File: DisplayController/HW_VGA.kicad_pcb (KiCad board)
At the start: 2 copper layers, 150 x 90 mm, 77 parts, among them J1 Conn_02x40_Odd_Even, J301 Conn_01x02, J401 Conn_01x06, U102 GAL22V10, U103 74ALS163, U104 74ALS163, U105 74ALS163, U202 GAL22V10, U203 74ALS163, U204 74ALS163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

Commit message: fixed one isolated ground
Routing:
- net GND: track 56.9 -> 60.8 mm, vias 45 -> 49
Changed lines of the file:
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@@
+	)
+	(via
+		(at 69 122.9)
+		(size 0.6)
+		(drill 0.3)
+		(layers "F.Cu" "B.Cu")
+		(free yes)
+		(net 2)
 	)
 	(via
@@
 	)
 	(via
+		(at 71.821 119.275)
+		(size 0.6)
+		(drill 0.3)
+		(layers "F.Cu" "B.Cu")
+		(net 2)
+	)
+	(via
+		(at 111.5 119.2)
+		(size 0.6)
+		(drill 0.3)
+		(layers "F.Cu" "B.Cu")
+		(net 2)
+	)
+	(via
 		(at 111.6 116.625)
 		(size 0.6)
@@
 	(via
 		(at 135.075 100.7)
+		(size 0.6)
+		(drill 0.3)
+		(layers "F.Cu" "B.Cu")
+		(free yes)
+		(net 2)
+	)
+	(via
+		(at 76.025 122.85)
 		(size 0.6)
 		(drill 0.3)
@@
 	)
 	(segment
+		(start 71.375 115.5725)
+		(end 71.375 118.829)
+		(width 0.6)
+		(layer "B.Cu")
+		(net 2)
+	)
+	(segment
 		(start 93.7575 121.4675)
 		(end 93.725 121.5)
 		(width 0.6)
 		(layer "B.Cu")
+		(net 2)
+	)
+	(segment
+		(start 71.375 118.829)
+		(end 71.821 119.275)
+		(width 0.6)
+		(layer "B.Cu")

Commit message: fix more unconnected grounds
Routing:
- net GND: track 60.8 -> 62.9 mm, vias 49 -> 60
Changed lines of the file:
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@@
+	)
+	(segment
+		(start 191.625 118.078001)
+		(end 191.6 118.103001)
+		(width 0.6)
+		(layer "F.Cu")
+		(net 2)
 	)
 	(segment
@@
 	)
 	(segment
+		(start 191.625 117.56)
+		(end 191.625 118.078001)
+		(width 0.6)
+		(layer "F.Cu")
+		(net 2)
+	)
+	(segment
 		(start 176.925 111.25)
 		(end 176.925 110.577)
@@
 	)
 	(segment
+		(start 191.625 120.1)
+		(end 193.2 120.1)
+		(width 0.6)
+		(layer "F.Cu")
+		(net 2)
+	)
+	(segment
 		(start 117.5 116.625)
 		(end 111.6 116.625)
@@
 	)
 	(via
+		(at 161.85 135.125)
+		(size 0.6)
+		(drill 0.3)
+		(layers "F.Cu" "B.Cu")
+		(free yes)
+		(net 2)
+	)
+	(via
 		(at 175.1 88.75)
 		(size 0.6)
@@
 	)
 	(via
+		(at 193.2 120.1)
+		(size 0.6)
+		(drill 0.3)
+		(layers "F.Cu" "B.Cu")
+		(net 2)
+	)
+	(via
 		(at 204.7 113.625)
 		(size 0.6)
@@
 	)
 	(via
+		(at 192.525 115.025)
+		(size 0.6)
+		(drill 0.3)
+		(layers "F.Cu" "B.Cu")
+		(net 2)
+	)
+	(via
 		(at 93.725 121.5)
 		(size 0.6)
@@
 	)
 	(via
+		(at 162.05 128.95)
+		(size 0.6)
+		(drill 0.3)
+		(layers "F.Cu" "B.Cu")
+		(free yes)
+		(net 2)
+	)
+	(via
 		(at 131.425 102.05)
 		(size 0.6)
@@
 	)
 	(via
+		(at 162.55 108.775)
+		(size 0.6)
+		(drill 0.3)
+		(layers "F.Cu" "B.Cu")
+		(free yes)
+		(net 2)
+	)
+	(via
 		(at 202.35 118.103001)
 		(size 0.6)
@@
 	)
 	(via
+		(at 191.6 118.103001)
+		(size 0.6)
+		(drill 0.3)
+		(layers "F.Cu" "B.Cu")
+		(net 2)
+	)
+	(via
 		(at 76.025 122.85)
 		(size 0.6)
@@
 	)
 	(via
+		(at 162.525 113.075)
+		(size 0.6)
+		(drill 0.3)
+		(layers "F.Cu" "B.Cu")
+		(free yes)
+		(net 2)
+	)
+	(via
 		(at 117.5 116.625)
 		(size 0.6)
@@
 	)
 	(via
+		(at 165.45 135.125)
+		(size 0.6)
+		(drill 0.3)
+		(layers "F.Cu" "B.Cu")
+		(free yes)
+		(net 2)
+	)
+	(via
 		(at 185.275 128.725)
 		(size 0.6)
@@
 	)
 	(via
+		(at 162.425 117.625)
+		(size 0.6)
+		(drill 0.3)
+		(layers "F.Cu" "B.Cu")
+		(free yes)
+		(net 2)
+	)
+	(via
 		(at 179.45 128.725)
 		(size 0.6)
@@
 	)
 	(via
+		(at 165.45 128.925)
+		(size 0.6)
+		(drill 0.3)
+		(layers "F.Cu" "B.Cu")
+		(free yes)
+		(net 2)
+	)
+	(via
 		(at 138.175 100.75)
 		(size 0.6)
@@
 		(net 2)
 	)
+	(via
+		(at 192.45 113.75)
+		(size 0.6)
+		(drill 0.3)
+		(layers "F.Cu" "B.Cu")
+		(net 2)
+	)

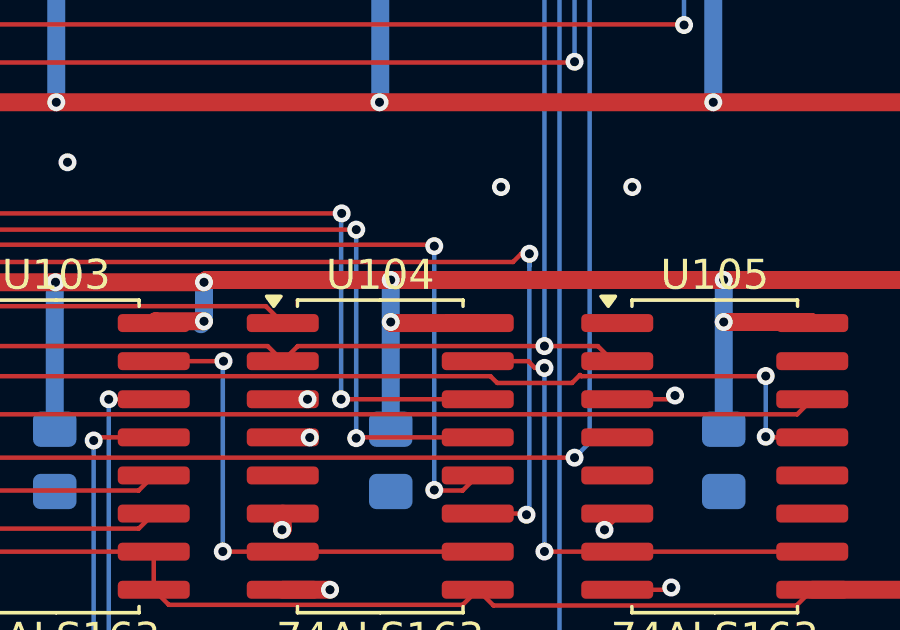
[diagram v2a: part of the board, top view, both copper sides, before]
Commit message: fixed a missing signal
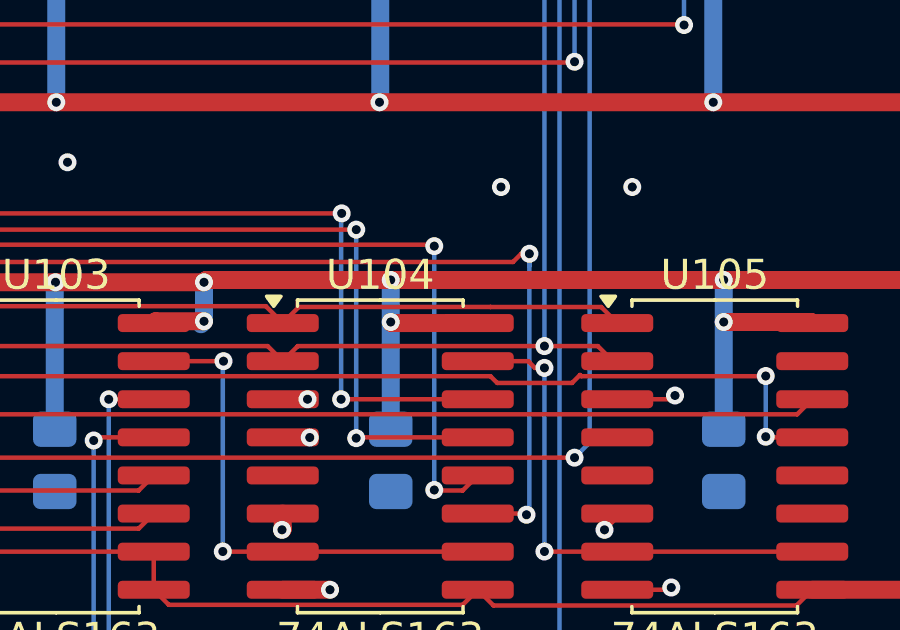
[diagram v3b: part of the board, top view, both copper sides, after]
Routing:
- net /HCount/-HCOUNT_CLR: track 26.7 -> 38.3 mm
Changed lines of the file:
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@@
+	)
+	(segment
+		(start 202.24 110.675)
+		(end 202.775 111.21)
+		(width 0.15)
+		(layer "F.Cu")
+		(net 108)
 	)
 	(segment
@@
 		(start 169.956 111.752)
 		(end 169.954 111.75)
+		(width 0.15)
+		(layer "F.Cu")
+		(net 108)
+	)
+	(segment
+		(start 198.548 110.673)
+		(end 198.55 110.675)
 		(width 0.15)
 		(layer "F.Cu")
@@
 	)
 	(segment
+		(start 198.55 110.675)
+		(end 202.24 110.675)
+		(width 0.15)
+		(layer "F.Cu")
+		(net 108)
+	)
+	(segment
+		(start 192.162 110.673)
+		(end 198.548 110.673)
+		(width 0.15)
+		(layer "F.Cu")
+		(net 108)
+	)
+	(segment
 		(start 191.063 110.648)
 		(end 181.387 110.648)
@@
 		(width 0.15)
 		(layer "F.Cu")
+		(net 108)
+	)
+	(segment
+		(start 191.625 111.21)
+		(end 192.162 110.673)
+		(width 0.15)
+		(layer "F.Cu")

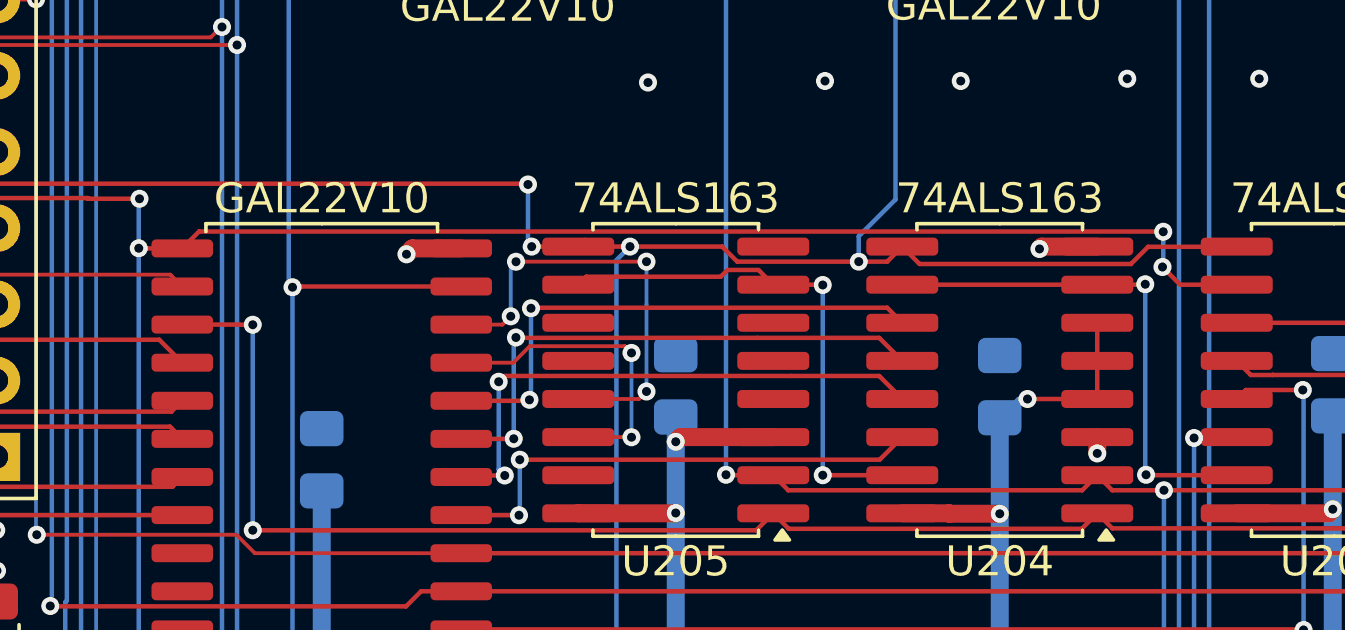
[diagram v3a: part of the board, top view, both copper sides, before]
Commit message: fix more unconnected grounds
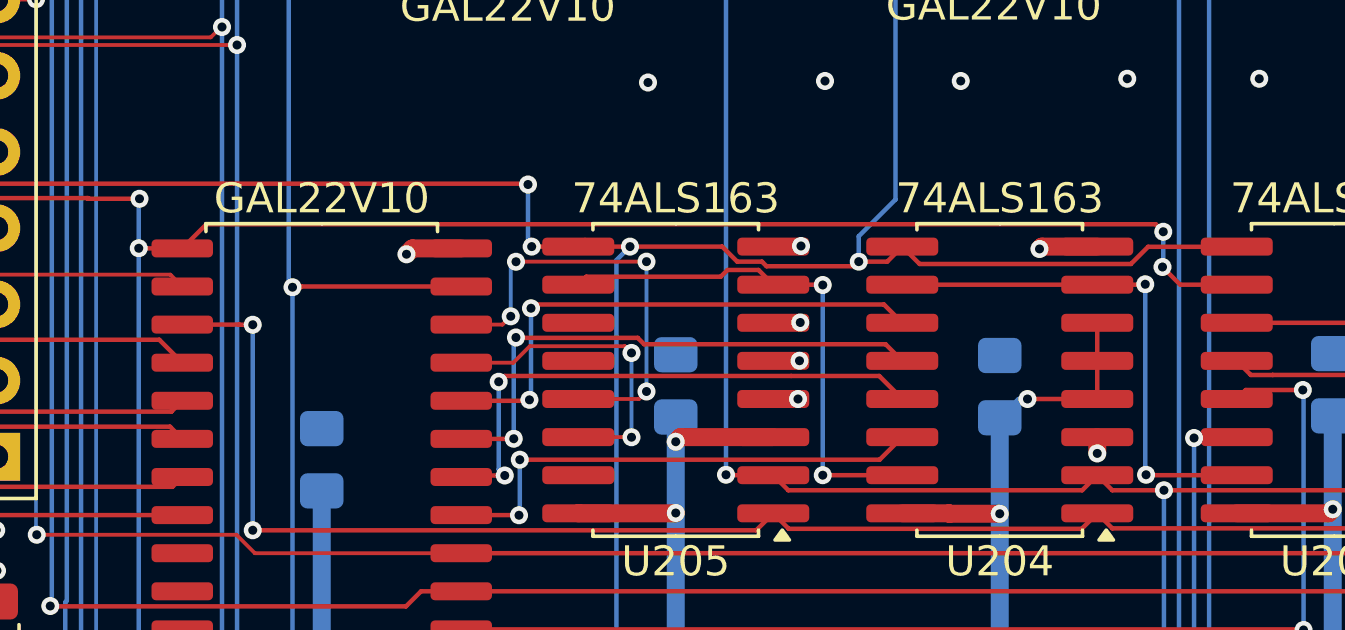
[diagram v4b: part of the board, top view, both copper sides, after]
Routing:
- net GND: vias 60 -> 64
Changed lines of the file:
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@@
 	)
 	(via
+		(at 188.25 88.475)
+		(size 0.6)
+		(drill 0.3)
+		(layers "F.Cu" "B.Cu")
+		(net 2)
+	)
+	(via
+		(at 188.225 91.025)
+		(size 0.6)
+		(drill 0.3)
+		(layers "F.Cu" "B.Cu")
+		(net 2)
+	)
+	(via
 		(at 130.3 96.45)
 		(size 0.6)
@@
 	)
 	(via
+		(at 188.15 93.575)
+		(size 0.6)
+		(drill 0.3)
+		(layers "F.Cu" "B.Cu")
+		(net 2)
+	)
+	(via
 		(at 189.05 82.975)
 		(size 0.6)
@@
 	)
 	(via
+		(at 188.2 92.3)
+		(size 0.6)
+		(drill 0.3)
+		(layers "F.Cu" "B.Cu")
+		(net 2)
+	)
+	(via
 		(at 199.2 124.125)
 		(size 0.6)
@@
 	)
 	(segment
-		(start 185.63902 88.51098)
-		(end 185.62304 88.495)
+		(start 127.69806 86.373)
+		(end 127.684962 86.359902)
 		(width 0.15)
 		(layer "F.Cu")
@@
 	)
 	(segment
-		(start 127.69806 86.373)
-		(end 127.684962 86.359902)
+		(start 112.7 67.85)
+		(end 127.675 67.85)
 		(width 0.15)
 		(layer "F.Cu")
@@
 	)
 	(segment
-		(start 112.7 67.85)
-		(end 127.675 67.85)
+		(start 190.175 88.997)
+		(end 190.022 89.15)
 		(width 0.15)
 		(layer "F.Cu")
@@
 	)
 	(segment
+		(start 190.022 89.15)
+		(end 187.101738 89.15)
+		(width 0.15)
+		(layer "F.Cu")
+		(net 65)
+	)
+	(segment
 		(start 182.55 88.495)
 		(end 182.555 88.5)
@@
 	)
 	(segment
-		(start 127.675 67.85)
-		(end 127.7 67.875)
+		(start 187.101738 89.15)
+		(end 186.948738 88.997)
 		(width 0.15)
 		(layer "F.Cu")
@@
 	)
 	(segment
-		(start 190.175 88.997)
-		(end 186.12504 88.997)
+		(start 186.12504 88.997)
+		(end 185.62304 88.495)
+		(width 0.15)
+		(layer "F.Cu")
+		(net 65)
+	)
+	(segment
+		(start 127.675 67.85)
+		(end 127.7 67.875)
 		(width 0.15)
 		(layer "F.Cu")
@@
 	)
 	(segment
+		(start 186.948738 88.997)
+		(end 186.12504 88.997)
+		(width 0.15)
+		(layer "F.Cu")
+		(net 65)
+	)
+	(segment
 		(start 191.123 88.997)
 		(end 190.175 88.997)
@@
 	)
 	(segment
-		(start 186.12504 88.997)
-		(end 185.63902 88.51098)
-		(width 0.15)
-		(layer "F.Cu")
-		(net 65)
-	)
-	(segment
 		(start 190.025 64.83)
 		(end 189.543 64.348)
@@
 	)
 	(segment
-		(start 185.62304 88.495)
-		(end 182.55 88.495)
-		(width 0.15)
-		(layer "F.Cu")
-		(net 65)
-	)
-	(segment
 		(start 158.125 86.375)
 		(end 158.123 86.373)
@@
 		(net 65)
 	)
+	(segment
+		(start 185.62304 88.495)
+		(end 182.55 88.495)
+		(width 0.15)
+		(layer "F.Cu")
+		(net 65)
+	)
 	(via
 		(at 112.723 76.275)
@@
 	)
 	(segment
-		(start 164.45 86.878)
-		(end 128.201 86.878)
-		(width 0.15)
-		(layer "F.Cu")
-		(net 105)
-	)
-	(segment
-		(start 168.187 87.993)
-		(end 200.318 87.993)
+		(start 168.43 87.75)
+		(end 200.075 87.75)
 		(width 0.15)
 		(layer "F.Cu")
@@
 	)
 	(segment
-		(start 200.318 87.993)
-		(end 200.325 88)
+		(start 164.45 86.878)
+		(end 128.201 86.878)
 		(width 0.15)
 		(layer "F.Cu")
@@
 	)
 	(segment
+		(start 200.075 87.75)
+		(end 200.325 88)
+		(width 0.15)
+		(layer "F.Cu")
+		(net 105)
+	)
+	(segment
 		(start 166.2 86.9)
 		(end 164.472 86.9)
@@
 	)
 	(segment
-		(start 200.3 89.175)
-		(end 200.89 89.765)
+		(start 167.625 88.555)
+		(end 168.43 87.75)
 		(width 0.15)
 		(layer "F.Cu")
@@
 	)
 	(segment
-		(start 167.625 88.555)
-		(end 168.187 87.993)
+		(start 200.3 89.175)
+		(end 200.89 89.765)
 		(width 0.15)
 		(layer "F.Cu")
@@
 	(segment
 		(start 191.625 91.035)
-		(end 191.123 90.533)
+		(end 191.015 90.425)
 		(width 0.15)
 		(layer "F.Cu")
@@
 	)
 	(segment
-		(start 191.123 90.533)
-		(end 179.267 90.533)
+		(start 179.165902 93.635)
+		(end 176.925 93.635)
 		(width 0.15)
 		(layer "F.Cu")
@@
 	)
 	(segment
-		(start 179.165902 93.635)
-		(end 176.925 93.635)
+		(start 179.198001 93.602901)
+		(end 179.165902 93.635)
 		(width 0.15)
 		(layer "F.Cu")
@@
 	)
 	(segment
-		(start 179.267 90.533)
-		(end 179.25 90.55)
+		(start 191.015 90.425)
+		(end 179.375 90.425)
 		(width 0.15)
 		(layer "F.Cu")
@@
 	)
 	(segment
-		(start 179.198001 93.602901)
-		(end 179.165902 93.635)
+		(start 179.375 90.425)
+		(end 179.25 90.55)
 		(width 0.15)
 		(layer "F.Cu")
@@
 	)
 	(segment
-		(start 178.76 91.537)
-		(end 178.748 91.525)
+		(start 182.807936 91.537)
+		(end 178.76 91.537)
 		(width 0.15)
 		(layer "F.Cu")
@@
 	)
 	(segment
-		(start 186.8 91.537)
-		(end 178.76 91.537)
+		(start 191.625 92.305)
+		(end 191.07 91.75)
 		(width 0.15)
 		(layer "F.Cu")
@@
 	)
 	(segment
-		(start 190.857 91.537)
-		(end 186.8 91.537)
+		(start 183.020936 91.75)
+		(end 182.807936 91.537)
 		(width 0.15)
 		(layer "F.Cu")
@@
 	)
 	(segment
-		(start 191.625 92.305)
-		(end 190.857 91.537)
+		(start 191.07 91.75)
+		(end 183.020936 91.75)
+		(width 0.15)
+		(layer "F.Cu")
+		(net 126)
+	)
+	(segment
+		(start 178.76 91.537)
+		(end 178.748 91.525)
 		(width 0.15)
 		(layer "F.Cu")

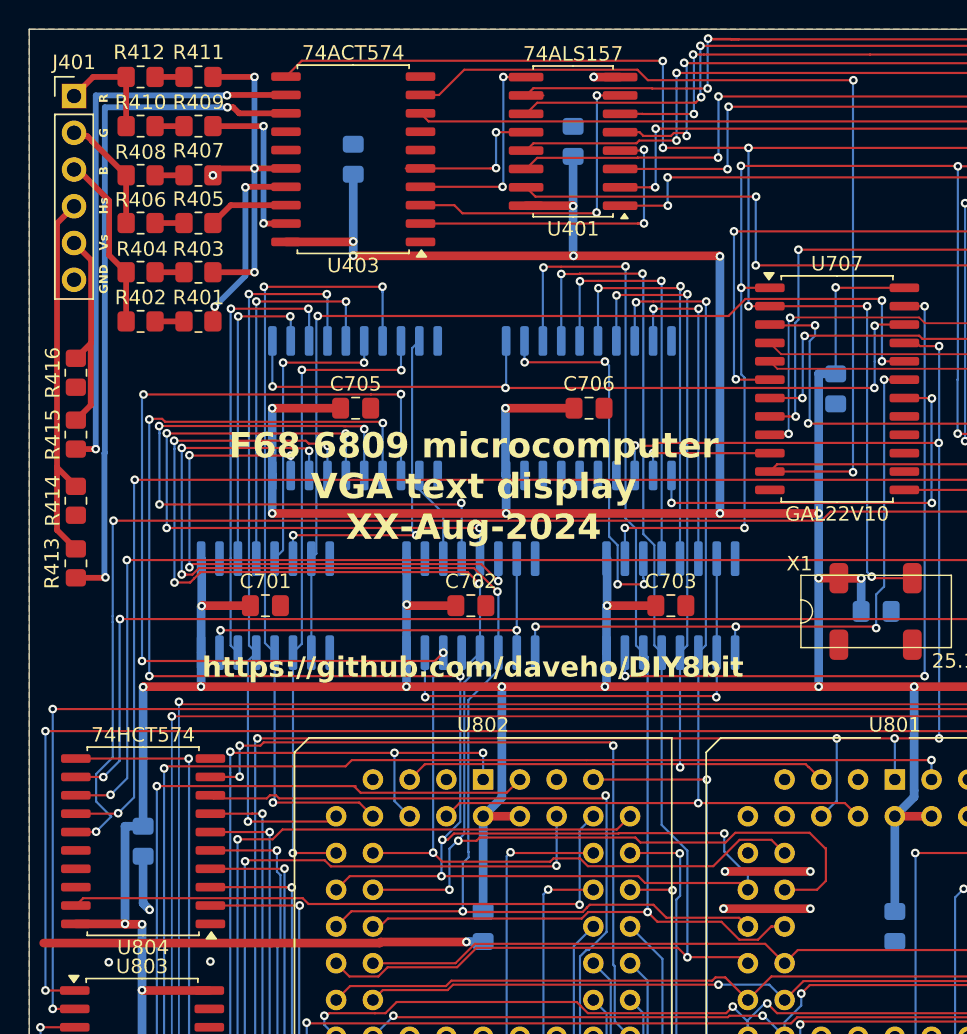
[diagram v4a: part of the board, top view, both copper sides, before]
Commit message: fixing more unrouted ground connections
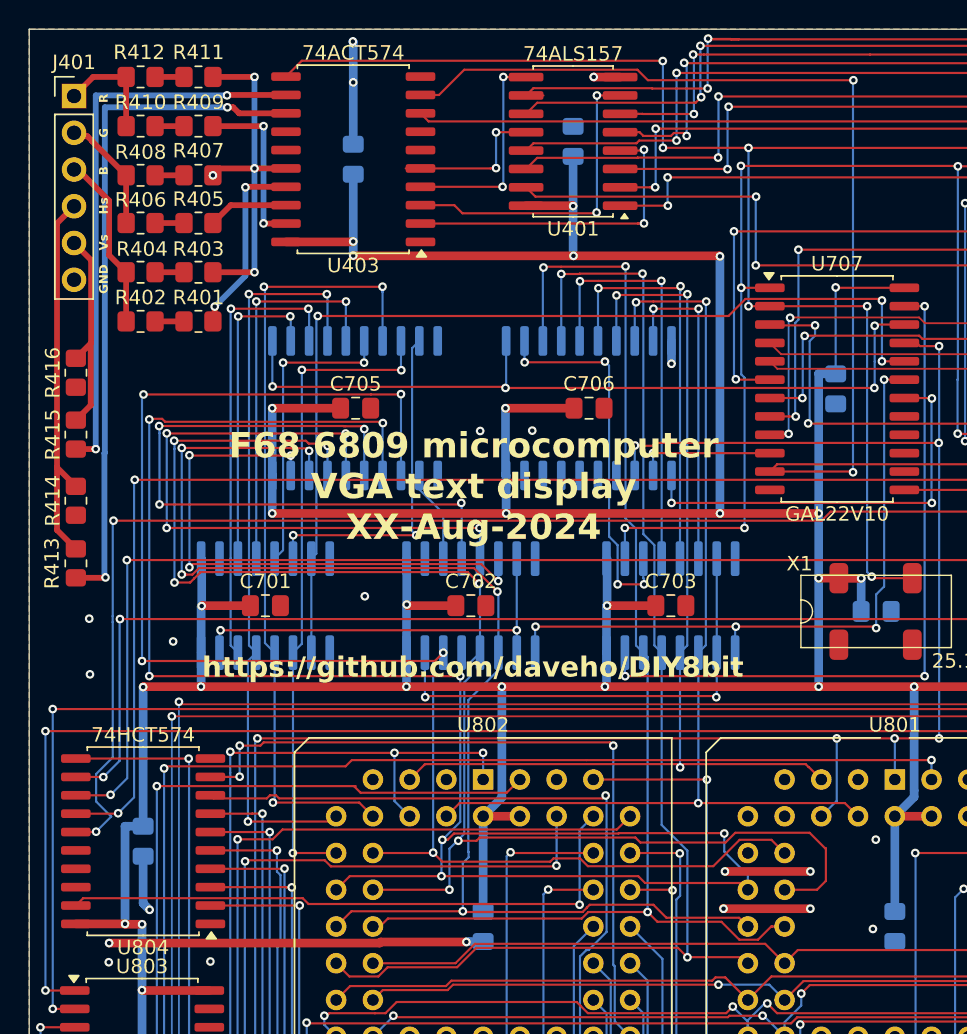
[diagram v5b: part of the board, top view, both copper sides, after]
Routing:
- net GND: track 62.9 -> 67.1 mm, vias 64 -> 76
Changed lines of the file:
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@@
-	)
-	(segment
-		(start 93.725 121.5)
-		(end 87.799658 121.5)
-		(width 0.6)
-		(layer "F.Cu")
-		(net 2)
 	)
 	(segment
@@
 	)
 	(segment
+		(start 87.799658 121.5)
+		(end 87.724658 121.575)
+		(width 0.6)
+		(layer "F.Cu")
+		(net 2)
+	)
+	(segment
 		(start 198.125 94.845)
 		(end 198.125 95.388001)
-		(width 0.6)
-		(layer "F.Cu")
-		(net 2)
-	)
-	(segment
-		(start 87.799658 121.5)
-		(end 87.724658 121.575)
 		(width 0.6)
 		(layer "F.Cu")
@@
 	)
 	(segment
+		(start 93.725 121.5)
+		(end 87.799658 121.5)
+		(width 0.6)
+		(layer "F.Cu")
+		(net 2)
+	)
+	(segment
 		(start 202.775 117.678001)
 		(end 202.35 118.103001)
@@
 	)
 	(segment
-		(start 80.25 121.575)
-		(end 64.5 121.575)
-		(width 0.6)
-		(layer "F.Cu")
-		(net 2)
-	)
-	(segment
-		(start 87.724658 121.575)
-		(end 80.25 121.575)
-		(width 0.6)
-		(layer "F.Cu")
-		(net 2)
-	)
-	(segment
 		(start 117.5 119.2)
 		(end 111.5 119.2)
@@
 		(net 2)
 	)
+	(segment
+		(start 69.025 121.575)
+		(end 87.724658 121.575)
+		(width 0.6)
+		(layer "F.Cu")
+		(net 2)
+	)
 	(via
 		(at 185.275 134.9)
@@
 	)
 	(via
+		(at 121.825 120.6)
+		(size 0.6)
+		(drill 0.3)
+		(layers "F.Cu" "B.Cu")
+		(free yes)
+		(net 2)
+	)
+	(via
 		(at 188.225 91.025)
 		(size 0.6)
@@
 	)
 	(via
+		(at 98.275 86.15)
+		(size 0.6)
+		(drill 0.3)
+		(layers "F.Cu" "B.Cu")
+		(free yes)
+		(net 2)
+	)
+	(via
+		(at 67.65 99.15)
+		(size 0.6)
+		(drill 0.3)
+		(layers "F.Cu" "B.Cu")
+		(free yes)
+		(net 2)
+	)
+	(via
+		(at 94.675 86.175)
+		(size 0.6)
+		(drill 0.3)
+		(layers "F.Cu" "B.Cu")
+		(free yes)
+		(net 2)
+	)
+	(via
 		(at 130.3 96.45)
 		(size 0.6)
@@
 	)
 	(via
+		(at 122.025 114.425)
+		(size 0.6)
+		(drill 0.3)
+		(layers "F.Cu" "B.Cu")
+		(free yes)
+		(net 2)
+	)
+	(via
 		(at 161.85 135.125)
 		(size 0.6)
@@
 	)
 	(via
+		(at 73.45 100.725)
+		(size 0.6)
+		(drill 0.3)
+		(layers "F.Cu" "B.Cu")
+		(free yes)
+		(net 2)
+	)
+	(via
 		(at 204.575 120.025)
 		(size 0.6)
@@
 	)
 	(via
+		(at 107.9 81.525)
+		(size 0.6)
+		(drill 0.3)
+		(layers "F.Cu" "B.Cu")
+		(net 2)
+	)
+	(via
 		(at 93.725 121.5)
 		(size 0.6)
@@
 	)
 	(via
+		(at 67.7 103)
+		(size 0.6)
+		(drill 0.3)
+		(layers "F.Cu" "B.Cu")
+		(free yes)
+		(net 2)
+	)
+	(via
 		(at 184.45 105.85)
 		(size 0.6)
@@
 	)
 	(via
+		(at 86.7 97.6)
+		(size 0.6)
+		(drill 0.3)
+		(layers "F.Cu" "B.Cu")
+		(free yes)
+		(net 2)
+	)
+	(via
+		(at 85.9 62.075)
+		(size 0.6)
+		(drill 0.3)
+		(layers "F.Cu" "B.Cu")
+		(net 2)
+	)
+	(via
 		(at 202.35 118.103001)
 		(size 0.6)
@@
 	)
 	(via
+		(at 85.875 59.25)
+		(size 0.6)
+		(drill 0.3)
+		(layers "F.Cu" "B.Cu")
+		(net 2)
+	)
+	(via
 		(at 203.125 128.15)
 		(size 0.6)
@@
 	)
 	(via
+		(at 69.025 121.575)
+		(size 0.6)
+		(drill 0.3)
+		(layers "F.Cu" "B.Cu")
+		(net 2)
+	)
+	(via
 		(at 162.525 113.075)
 		(size 0.6)
@@
 		(net 2)
 	)
+	(segment
+		(start 107.9 79.95)
+		(end 107.9 81.525)
+		(width 0.6)
+		(layer "B.Cu")
+		(net 2)
+	)
+	(segment
+		(start 85.9 66.3525)
+		(end 85.9 59.275)
+		(width 0.6)
+		(layer "B.Cu")
+		(net 2)
+	)
+	(segment
+		(start 85.9 59.275)
+		(end 85.875 59.25)
+		(width 0.6)
+		(layer "B.Cu")
+		(net 2)
+	)
